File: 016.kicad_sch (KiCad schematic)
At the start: 3 parts, among them P1 Header 2x18 2.54mm, P2 Header 2x18 2.54mm

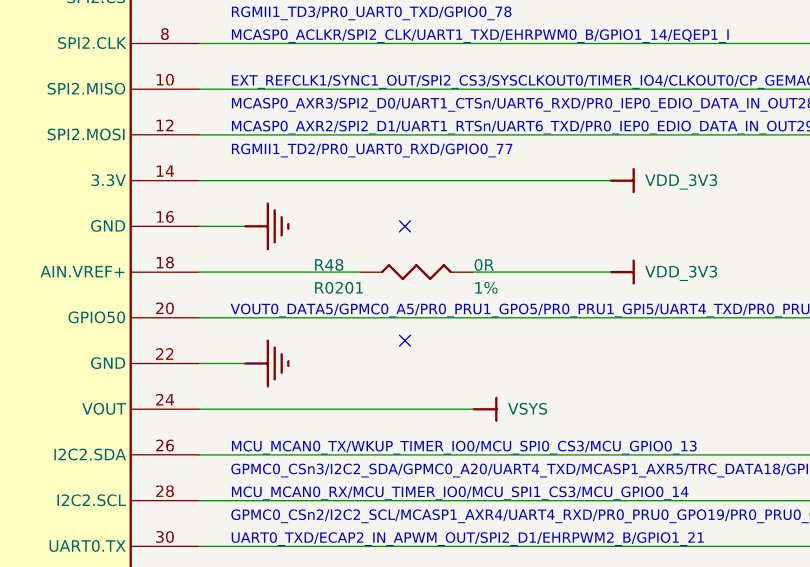
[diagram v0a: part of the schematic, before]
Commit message: Remove rando NCs added during conversion
Also a little tidying.

TODO: check junctions that may be missing. Noticed a few obvious ones
and corrected them already.

Signed-off-by: Michael Welling <mwelling79@gmail.com>
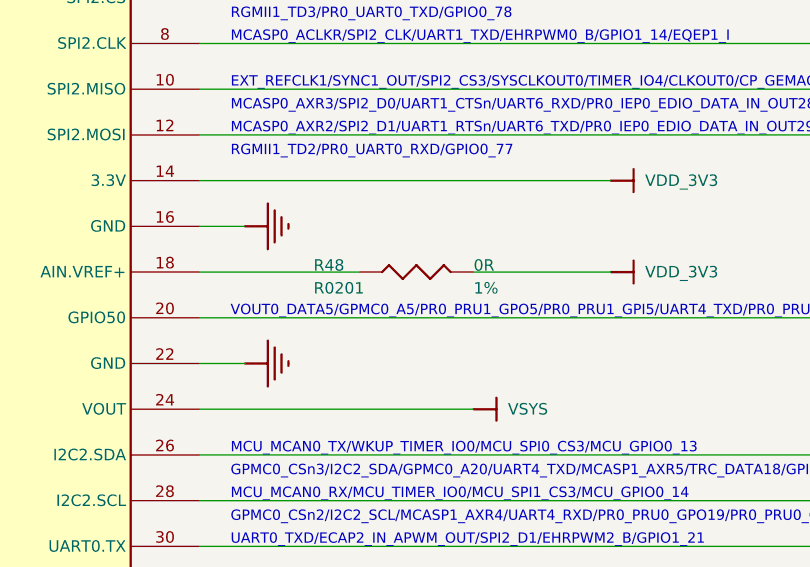
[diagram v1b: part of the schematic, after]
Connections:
- no-connect marks 2 -> 0
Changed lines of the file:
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@@
 		(color 0 0 0 0)
-	)
-	(no_connect
-		(at 254 63.5)
-	)
-	(no_connect
-		(at 254 76.2)
 	)
 	(wire
